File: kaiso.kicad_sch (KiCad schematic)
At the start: 404 parts, among them J1 Conn_01x04, J2 Conn_01x05, J3 Conn_01x02, J4 Conn_01x02, SW0_18 Mechanical_Switch, SW0_19 Mechanical_Switch, SW0_20 Mechanical_Switch, SW0_21 Mechanical_Switch, SW0_22 Mechanical_Switch, SW0_23 Mechanical_Switch, SW0_24 Mechanical_Switch, SW0_25 Mechanical_Switch, SW0_26 Mechanical_Switch, SW0_27 Mechanical_Switch, SW0_28 Mechanical_Switch, SW0_29 Mechanical_Switch, SW0_30 Mechanical_Switch, SW0_31 Mechanical_Switch, SW0_32 Mechanical_Switch, SW0_33 Mechanical_Switch, SW0_34 Mechanical_Switch, SW0_35 Mechanical_Switch, SW1_14 Mechanical_Switch, SW1_18 Mechanical_Switch, SW1_19 Mechanical_Switch, SW1_20 Mechanical_Switch, SW1_21 Mechanical_Switch, SW1_22 Mechanical_Switch, SW1_23 Mechanical_Switch, SW1_24 Mechanical_Switch, SW1_25 Mechanical_Switch, SW1_26 Mechanical_Switch, SW1_27 Mechanical_Switch, SW1_28 Mechanical_Switch, SW1_29 Mechanical_Switch, SW1_30 Mechanical_Switch, SW1_31 Mechanical_Switch, SW1_32 Mechanical_Switch, SW1_33 Mechanical_Switch, SW2_14 Mechanical_Switch, SW2_18 Mechanical_Switch, SW2_19 Mechanical_Switch, SW2_20 Mechanical_Switch, SW2_21 Mechanical_Switch, SW2_22 Mechanical_Switch, SW2_23 Mechanical_Switch, SW2_24 Mechanical_Switch, SW2_25 Mechanical_Switch, SW2_26 Mechanical_Switch, SW2_27 Mechanical_Switch, SW2_28 Mechanical_Switch, SW2_29 Mechanical_Switch, SW2_30 Mechanical_Switch, SW2_31 Mechanical_Switch, SW2_32 Mechanical_Switch, SW2_33 Mechanical_Switch, SW3_13 Mechanical_Switch, SW3_14 Mechanical_Switch, SW3_18 Mechanical_Switch, SW3_19 Mechanical_Switch, SW3_20 Mechanical_Switch, SW3_21 Mechanical_Switch, SW3_22 Mechanical_Switch, SW3_23 Mechanical_Switch, SW3_24 Mechanical_Switch, SW3_25 Mechanical_Switch, SW3_26 Mechanical_Switch, SW3_27 Mechanical_Switch, SW3_28 Mechanical_Switch, SW3_29 Mechanical_Switch, SW3_30 Mechanical_Switch, SW3_31 Mechanical_Switch, SW4_11 Mechanical_Switch, SW4_14 Mechanical_Switch, SW4_18 Mechanical_Switch, SW4_19 Mechanical_Switch, SW4_20 Mechanical_Switch, SW4_21 Mechanical_Switch, SW4_22 Mechanical_Switch, SW4_23 Mechanical_Switch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

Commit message: Finished the schematic REV 1
Still need to update the switch schematic symbol and double check the boot and reset pins
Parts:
- removed J2: Conn_01x05, symbol Connector_Generic:Conn_01x05
- added C10, C11: 1uF, symbol Device:C
- added C12, C13: 10pF, symbol Device:C
- added C9: 10nF, symbol Device:C
- added D1: RED, symbol Device:LED
- added FB1: 120R, symbol Device:FerriteBead
- added J2: Conn_01x04_Pin, symbol Connector:Conn_01x04_Pin
- added R3: 1.5k, symbol Device:R_US
- added Y1: 16MHz, symbol Device:Crystal_GND24
- J1: value Conn_01x04 -> JST_SH_Conn_01x04; footprint Connector_Molex:Molex_Pico-EZmate_78171-0004_1x04-1MP_P1.20mm_Vertical -> Connector_JST:JST_SH_BM04B-SRSS-TB_1x04-1MP_P1.00mm_Vertical
- LED1: value SK6812MINI-E -> Esc
- LED10: value SK6812MINI-E -> F9
- LED100: value SK6812MINI-E -> Fn
- LED101, LED91: value SK6812MINI-E -> Ctrl
- LED103: value SK6812MINI-E -> Left
- LED104: value SK6812MINI-E -> Down
- LED106: value SK6812MINI-E -> Right
- LED107, LED29: value SK6812MINI-E -> 0
- LED108: value SK6812MINI-E -> .
- LED11: value SK6812MINI-E -> F10
- LED12: value SK6812MINI-E -> F11
- LED13: value SK6812MINI-E -> F12
- LED14: value SK6812MINI-E -> Home/End
- LED15: value SK6812MINI-E -> Del/Ins
- LED16: value SK6812MINI-E -> PgUp/PgDn
- LED17, LED83: value SK6812MINI-E -> /
- LED18: value SK6812MINI-E -> *
- LED19: value SK6812MINI-E -> `
- LED2: value SK6812MINI-E -> F1
- LED20, LED88: value SK6812MINI-E -> 1
- LED21, LED89: value SK6812MINI-E -> 2
- LED22, LED90: value SK6812MINI-E -> 3
- LED23, LED70: value SK6812MINI-E -> 4
- LED24, LED71: value SK6812MINI-E -> 5
- LED25, LED72: value SK6812MINI-E -> 6
- LED26, LED52: value SK6812MINI-E -> 7
- LED27, LED53: value SK6812MINI-E -> 8
- LED28, LED54: value SK6812MINI-E -> 9
- LED3: value SK6812MINI-E -> F2
- LED30, LED36: value SK6812MINI-E -> -
- LED31: value SK6812MINI-E -> =
- LED32: value SK6812MINI-E -> Backspace
- LED34: value SK6812MINI-E -> Num Lk
- LED35: value SK6812MINI-E -> +
- LED37: value SK6812MINI-E -> Tab
- LED38: value SK6812MINI-E -> q
- LED39: value SK6812MINI-E -> w
- LED4: value SK6812MINI-E -> F3
- LED40: value SK6812MINI-E -> e
- LED41: value SK6812MINI-E -> r
- LED42: value SK6812MINI-E -> t
- LED43: value SK6812MINI-E -> y
- LED44: value SK6812MINI-E -> u
- LED45: value SK6812MINI-E -> i
- LED46: value SK6812MINI-E -> o
- LED47: value SK6812MINI-E -> P
- LED48: value SK6812MINI-E -> [
- LED49: value SK6812MINI-E -> ]
- LED5: value SK6812MINI-E -> F4
- LED50: value SK6812MINI-E -> Enter
- LED55: value SK6812MINI-E -> Caps Lock
- LED56: value SK6812MINI-E -> a
- LED57: value SK6812MINI-E -> s
- LED58: value SK6812MINI-E -> d
- LED59: value SK6812MINI-E -> f
- LED6: value SK6812MINI-E -> F5
- LED60: value SK6812MINI-E -> g
- LED61: value SK6812MINI-E -> h
- LED62: value SK6812MINI-E -> j
- LED63: value SK6812MINI-E -> k
- LED64: value SK6812MINI-E -> L
- LED65: value SK6812MINI-E -> ;
- LED66: value SK6812MINI-E -> '
- LED67: value SK6812MINI-E -> \
- LED7: value SK6812MINI-E -> F6
- LED73, LED85: value SK6812MINI-E -> Shift
- LED74: value SK6812MINI-E -> z
- LED75: value SK6812MINI-E -> x
- LED76: value SK6812MINI-E -> c
- LED77: value SK6812MINI-E -> v
- LED78: value SK6812MINI-E -> b
- LED79: value SK6812MINI-E -> n
- LED8: value SK6812MINI-E -> F7
- LED80: value SK6812MINI-E -> m
- LED81: value SK6812MINI-E -> <
- LED82: value SK6812MINI-E -> >
- LED86: value SK6812MINI-E -> Up
- LED9: value SK6812MINI-E -> F8
- LED92: value SK6812MINI-E -> Super
- LED93, LED99: value SK6812MINI-E -> Alt
- LED96: value SK6812MINI-E -> Space
- SW0_18: Keycode ESC -> KC
- SW5_23: Keycode . Prt Sc -> KC
- SW5_4: Keycode Win -> KC
- SW5_6: Keycode Alt -> KC
- U1: value STM32F103C8Tx -> STM32F103C8T6
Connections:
- net INTB is gone; now on net COL6: U1.25 (PB12)
- net SCL is gone; now on net COL4: U1.21 (PB10)
- net SDA is gone; now on net COL5: U1.22 (PB11)
- net SDB is gone; now on net COL7: U1.26 (PB13)
- net +3.3V: now also C11.1, D1.2 (A), FB1.2, J2.1 (Pin_1); no longer U1.9 (VDDA)
- net COL0: no longer SW0_18.1
- net COL1: no longer SW5_4.1
- net COL10: now also U1.10 (PA0); no longer U1.14 (PA4)
- net COL11: now also U1.11 (PA1); no longer U1.15 (PA5)
- net COL12: now also U1.12 (PA2); no longer U1.16 (PA6)
- net COL13: now also U1.13 (PA3); no longer U1.17 (PA7)
- net COL14: now also U1.14 (PA4); no longer U1.29 (PA8)
- net COL15: now also U1.15 (PA5); no longer U1.30 (PA9)
- net COL16: now also U1.16 (PA6); no longer U1.31 (PA10)
- net COL17: now also U1.17 (PA7); no longer SW0_35.1, U1.38 (PA15)
- net COL4: no longer U1.27 (PB14)
- net COL5: no longer U1.28 (PB15)
- net COL6: no longer U1.10 (PA0)
- net COL7: no longer U1.11 (PA1)
- net COL8: now also U1.27 (PB14); no longer U1.12 (PA2)
- net COL9: now also U1.28 (PB15); no longer U1.13 (PA3)
- net GND: now also C10.2, C11.2, C12.2, C13.2, C9.2, J2.4 (Pin_4), R3.2, Y1.2, Y1.4
- net RGB: now also U1.30 (PA9)
- net SWCLK: now also J2.3 (Pin_3)
- net SWDIO: now also J2.2 (Pin_2)
- net HSE_IN: now reaches U1.5 (PD0)
- net HSE_IN: now also C12.1, Y1.1
- net HSE_OUT: now reaches U1.6 (PD1)
- net HSE_OUT: now also C13.1, Y1.3
- net at D90.2 (A): no longer SW5_4.2
- net at D24.2 (A): no longer SW0_18.2
- net D+ renamed USB_D+
- net D- renamed USB_D-
- new net: D1.1 (K), R3.1
- new net +3.3VA: C10.1, C9.1, FB1.1, U1.9 (VDDA)
- no-connect marks 0 -> 7
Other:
- removed sheet LED_Matrix
- note added: "CL=2*(CL0-Cs)=2*(10-5)pF=10pF"
- note added: "Crystal Oscillator"
- note added: "Decoupling Capacitor for VA"
- note removed: "Switch Matrix"
- title: KiKeeb -> Kaiso92
- moved on the sheet: C1, C100, C101, C103, C104, C105, C106, C107, C108, C111, C114, C115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

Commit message: updated the switch matrix symbols and fixed some violations.
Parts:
- removed D109, D110, D111, D112, D113, D114, D115, D116, D117, D118, D119, D120, D121, D122, D123, D124, D125, D126, D127, D128, D129, D130, D131, D132, D133, D134, D135, D136, D137, D138, D139, D140, D141, D142, D143, D144, D145, D146, D147, D148, D149, D150, D151, D152, D153, D154, D155, D156, D157, D158, D159, D160, D161, D162, D163, D164, D165, D166, D167, D168, D169, D170, D171, D172, D173, D174, D175, D176, D177, D178, D179, D180, D181, D182, D183, D184, D185, D186, D187, D188, D189, D190, D191, D192: 1N4148W, Diode_SMD:D_SOD-123, symbol Diode:1N4148W
- removed SW0_19, SW0_20, SW0_21, SW0_22, SW0_23, SW0_24, SW0_25, SW0_26, SW0_27, SW0_28, SW0_29, SW0_30, SW0_31, SW0_32, SW0_33, SW0_34, SW0_35, SW1_14, SW1_18, SW1_19, SW1_20, SW1_21, SW1_22, SW1_23, SW1_24, SW1_25, SW1_26, SW1_27, SW1_28, SW1_29, SW1_30, SW1_31, SW1_32, SW1_33, SW2_18, SW2_19, SW2_20, SW2_21, SW2_22, SW2_23, SW2_24, SW2_25, SW2_26, SW2_27, SW2_28, SW2_29, SW2_30, SW2_31, SW2_32, SW2_33, SW3_14, SW3_18, SW3_19, SW3_20, SW3_21, SW3_22, SW3_23, SW3_24, SW3_25, SW3_26, SW3_27, SW3_28, SW3_29, SW3_30, SW3_31, SW4_14, SW4_18, SW4_19, SW4_20, SW4_21, SW4_22, SW4_23, SW4_24, SW4_25, SW4_26, SW4_28, SW4_29, SW4_30, SW4_31, SW5_14, SW5_18, SW5_19, SW5_20, SW5_21, SW5_22, SW5_23, SW5_7: Mechanical_Switch, PCM_marbastlib-mx:SW_MX_1u, symbol acheron_Symbols:Mechanical_Switch
- removed SW2_14: Mechanical_Switch, PCM_marbastlib-mx:SW_MX_1.5u, symbol acheron_Symbols:Mechanical_Switch
- removed SW3_13, SW4_27: Mechanical_Switch, PCM_marbastlib-mx:SW_MX_1.75u, symbol acheron_Symbols:Mechanical_Switch
- removed SW5_3, SW5_4, SW5_6: Mechanical_Switch, PCM_marbastlib-mx:SW_MX_1.25u, symbol acheron_Symbols:Mechanical_Switch
- added D10, D11, D12, D13, D14, D15, D16, D17, D18, D19, D20, D21, D22, D23, D24, D25, D26, D27, D28, D29, D3, D31, D32, D33, D34, D35, D36, D37, D38, D39, D4, D40, D41, D43, D44, D45, D46, D47, D49, D5, D50, D51, D52, D53, D54, D55, D56, D57, D58, D59, D6, D60, D61, D62, D63, D64, D65, D66, D67, D68, D69, D7, D70, D73, D74, D75, D76, D77, D78, D79, D8, D80, D81, D83, D84, D85, D9, D91, D92, D93, D94, D95, D96, D97: 1N4148W, Diode_SMD:D_SOD-123, symbol Diode:1N4148W
- added SW0_1, SW0_10, SW0_11, SW0_12, SW0_13, SW0_14, SW0_15, SW0_16, SW0_17, SW0_2, SW0_3, SW0_4, SW0_5, SW0_6, SW0_7, SW0_8, SW0_9, SW1_0, SW1_1, SW1_10, SW1_11, SW1_12, SW1_13, SW1_15, SW1_16, SW1_17, SW1_2, SW1_3, SW1_4, SW1_5, SW1_6, SW1_7, SW1_8, SW1_9, SW2_1, SW2_10, SW2_11, SW2_12, SW2_13, SW2_15, SW2_16, SW2_17, SW2_2, SW2_3, SW2_4, SW2_5, SW2_6, SW2_7, SW2_8, SW2_9, SW3_1, SW3_10, SW3_11, SW3_12, SW3_15, SW3_16, SW3_17, SW3_2, SW3_3, SW3_4, SW3_5, SW3_6, SW3_7, SW3_8, SW3_9, SW4_0, SW4_1, SW4_10, SW4_12, SW4_15, SW4_16, SW4_17, SW4_2, SW4_3, SW4_4, SW4_5, SW4_6, SW4_7, SW4_8, SW4_9, SW5_10, SW5_12, SW5_15, SW5_16, SW5_17, SW5_5, SW5_8, SW5_9: Mechanical_Switch, PCM_marbastlib-mx:SW_MX_1u, symbol acheron_Symbols:Mechanical_Switch
- added SW2_0: Mechanical_Switch, PCM_marbastlib-mx:SW_MX_1.5u, symbol acheron_Symbols:Mechanical_Switch
- added SW3_0: Mechanical_Switch, PCM_marbastlib-mx:SW_MX_1.75u, symbol acheron_Symbols:Mechanical_Switch
- added SW5_0, SW5_1, SW5_2: Mechanical_Switch, PCM_marbastlib-mx:SW_MX_1.25u, symbol acheron_Symbols:Mechanical_Switch
- SW0_0: renamed from SW0_18; Keycode KC -> ESC
- SW4_11: footprint PCM_marbastlib-mx:SW_MX_1u -> PCM_marbastlib-mx:SW_MX_1.75u
- SW5_11: Keycode Alt -> Left
- renumbered D24 to D2
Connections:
- net COL0: now also SW0_0.1, SW1_0.1, SW2_0.1, SW3_0.1, SW4_0.1, SW5_0.1; no longer SW4_11.1
- net COL1: now also SW0_1.1, SW1_1.1, SW2_1.1, SW3_1.1, SW4_1.1, SW5_1.1
- net COL10: now also SW0_10.1, SW1_10.1, SW2_10.1, SW3_10.1, SW4_10.1, SW5_10.1
- net COL11: now also SW4_11.1, SW5_11.1, SW0_11.1, SW1_11.1, SW2_11.1, SW3_11.1
- net COL12: now also SW0_12.1, SW1_12.1, SW2_12.1, SW3_12.1, SW4_12.1, SW5_12.1
- net COL13: now also SW0_13.1, SW1_13.1, SW2_13.1
- net COL14: now also SW0_14.1
- net COL15: now also SW0_15.1, SW1_15.1, SW2_15.1, SW3_15.1, SW4_15.1, SW5_15.1
- net COL16: now also SW0_16.1, SW1_16.1, SW2_16.1, SW3_16.1, SW4_16.1, SW5_16.1
- net COL17: now also SW0_17.1, SW1_17.1, SW2_17.1, SW3_17.1, SW4_17.1, SW5_17.1
- net COL2: now also SW0_2.1, SW1_2.1, SW2_2.1, SW3_2.1, SW4_2.1, SW5_2.1
- net COL3: now also SW0_3.1, SW1_3.1, SW2_3.1, SW3_3.1, SW4_3.1
- net COL4: now also SW0_4.1, SW1_4.1, SW2_4.1, SW3_4.1, SW4_4.1
- net COL5: now also SW0_5.1, SW1_5.1, SW2_5.1, SW3_5.1, SW4_5.1, SW5_5.1
- net COL6: now also SW0_6.1, SW1_6.1, SW2_6.1, SW3_6.1, SW4_6.1
- net COL7: now also SW0_7.1, SW1_7.1, SW2_7.1, SW3_7.1, SW4_7.1
- net COL8: now also SW0_8.1, SW1_8.1, SW2_8.1, SW3_8.1, SW4_8.1, SW5_8.1; no longer SW5_11.1
- net COL9: now also SW0_9.1, SW1_9.1, SW2_9.1, SW3_9.1, SW4_9.1, SW5_9.1
- net ROW0: now also D10.1 (K), D11.1 (K), D12.1 (K), D13.1 (K), D14.1 (K), D15.1 (K), D16.1 (K), D17.1 (K), D18.1 (K), D19.1 (K), D3.1 (K), D4.1 (K), D5.1 (K), D6.1 (K), D7.1 (K), D8.1 (K), D9.1 (K); no longer D82.1 (K)
- net ROW1: now also D20.1 (K), D21.1 (K), D22.1 (K), D23.1 (K), D24.1 (K), D25.1 (K), D26.1 (K), D27.1 (K), D28.1 (K), D29.1 (K), D31.1 (K), D32.1 (K), D33.1 (K), D34.1 (K), D35.1 (K), D36.1 (K); no longer D86.1 (K)
- net ROW2: now also D48.1 (K), D37.1 (K), D38.1 (K), D39.1 (K), D40.1 (K), D41.1 (K), D43.1 (K), D44.1 (K), D45.1 (K), D46.1 (K), D47.1 (K), D49.1 (K), D50.1 (K), D51.1 (K), D52.1 (K), D53.1 (K); no longer D87.1 (K)
- net ROW3: now also D54.1 (K), D55.1 (K), D56.1 (K), D57.1 (K), D58.1 (K), D59.1 (K), D60.1 (K), D61.1 (K), D62.1 (K), D63.1 (K), D64.1 (K), D65.1 (K), D66.1 (K), D67.1 (K), D68.1 (K), D69.1 (K); no longer D48.1 (K), D88.1 (K)
- net ROW4: now also D72.1 (K), D82.1 (K), D70.1 (K), D73.1 (K), D74.1 (K), D75.1 (K), D76.1 (K), D77.1 (K), D78.1 (K), D79.1 (K), D80.1 (K), D81.1 (K), D83.1 (K), D84.1 (K), D85.1 (K); no longer D89.1 (K)
- net ROW5: now also D86.1 (K), D87.1 (K), D88.1 (K), D89.1 (K), D91.1 (K), D92.1 (K), D93.1 (K), D94.1 (K), D95.1 (K), D96.1 (K), D97.1 (K); no longer D72.1 (K)
- net at D87.2 (A): now also SW5_1.2
- net at D48.2 (A): now also SW2_11.2
- net at D82.2 (A): now also SW4_12.2
- net at D88.2 (A): now also SW5_2.2
- net at D42.2 (A): now also SW2_5.2
- net at D71.2 (A): now also SW4_1.2; no longer SW4_11.2
- net at D86.2 (A): now also SW5_0.2
- net at SW5_11.2: now also D93.2 (A)
- net at D89.2 (A): now also SW5_5.2
- net at D90.2 (A): now also SW5_8.2
- net at D2.2 (A): now also SW0_0.2
- net at D30.2 (A): now also SW1_10.2
- net at D72.2 (A): now also SW4_2.2
- new net: D38.2 (A), SW2_1.2
- new net: D36.2 (A), SW1_17.2
- new net: D76.2 (A), SW4_6.2
- new net: D43.2 (A), SW2_6.2
- new net: D27.2 (A), SW1_7.2
- new net: D75.2 (A), SW4_5.2
- new net: D17.2 (A), SW0_15.2
- new net: D78.2 (A), SW4_8.2
- new net: D51.2 (A), SW2_15.2
- new net: D74.2 (A), SW4_4.2
- new net: D10.2 (A), SW0_8.2
- new net: D60.2 (A), SW3_6.2
- new net: D85.2 (A), SW4_17.2
- new net: D35.2 (A), SW1_16.2
- new net: D97.2 (A), SW5_17.2
- new net: D8.2 (A), SW0_6.2
- new net: D32.2 (A), SW1_12.2
- new net: D21.2 (A), SW1_1.2
- new net: D39.2 (A), SW2_2.2
- new net: D24.2 (A), SW1_4.2
- new net: D70.2 (A), SW4_0.2
- new net: D47.2 (A), SW2_10.2
- new net: D50.2 (A), SW2_13.2
- new net: D96.2 (A), SW5_16.2
- new net: D81.2 (A), SW4_11.2
- new net: D34.2 (A), SW1_15.2
- new net: D80.2 (A), SW4_10.2
- new net: D4.2 (A), SW0_2.2
- new net: D49.2 (A), SW2_12.2
- new net: D46.2 (A), SW2_9.2
- new net: D22.2 (A), SW1_2.2
- new net: D91.2 (A), SW5_9.2
- new net: D77.2 (A), SW4_7.2
- new net: D25.2 (A), SW1_5.2
- new net: D59.2 (A), SW3_5.2
- new net: D41.2 (A), SW2_4.2
- new net: D53.2 (A), SW2_17.2
- new net: D45.2 (A), SW2_8.2
- new net: D92.2 (A), SW5_10.2
- new net: D6.2 (A), SW0_4.2
- new net: D95.2 (A), SW5_15.2
- new net: D64.2 (A), SW3_10.2
- new net: D20.2 (A), SW1_0.2
- new net: D83.2 (A), SW4_15.2
- new net: D37.2 (A), SW2_0.2
- new net: D40.2 (A), SW2_3.2
- new net: D54.2 (A), SW3_0.2
- new net: D28.2 (A), SW1_8.2
- new net: D11.2 (A), SW0_9.2
- new net: D73.2 (A), SW4_3.2
- new net: D13.2 (A), SW0_11.2
- new net: D5.2 (A), SW0_3.2
- new net: D12.2 (A), SW0_10.2
- new net: D44.2 (A), SW2_7.2
- new net: D7.2 (A), SW0_5.2
- new net: D18.2 (A), SW0_16.2
- new net: D33.2 (A), SW1_13.2
- new net: D3.2 (A), SW0_1.2
- new net: D19.2 (A), SW0_17.2
- new net: D69.2 (A), SW3_17.2
- new net: D94.2 (A), SW5_12.2
- new net: D29.2 (A), SW1_9.2
- new net: D66.2 (A), SW3_12.2
- new net: D15.2 (A), SW0_13.2
- new net: D56.2 (A), SW3_2.2
- new net: D23.2 (A), SW1_3.2
- new net: D61.2 (A), SW3_7.2
- new net: D14.2 (A), SW0_12.2
- new net: D31.2 (A), SW1_11.2
- new net: D62.2 (A), SW3_8.2
- new net: D79.2 (A), SW4_9.2
- new net: D57.2 (A), SW3_3.2
- new net: D52.2 (A), SW2_16.2
- new net: D58.2 (A), SW3_4.2
- new net: D67.2 (A), SW3_15.2
- new net: D84.2 (A), SW4_16.2
- new net: D63.2 (A), SW3_9.2
- new net: D55.2 (A), SW3_1.2
- new net: D65.2 (A), SW3_11.2
- new net: D26.2 (A), SW1_6.2
- new net: D68.2 (A), SW3_16.2
- new net: D16.2 (A), SW0_14.2
- new net: D9.2 (A), SW0_7.2
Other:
- note added: "SK6812mini-e LED Chain"
- note added: "Switch Matrix"
- moved on the sheet: C1, C10, C100, C101, C103, C104, C105, C106, C107, C108, C11, C111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

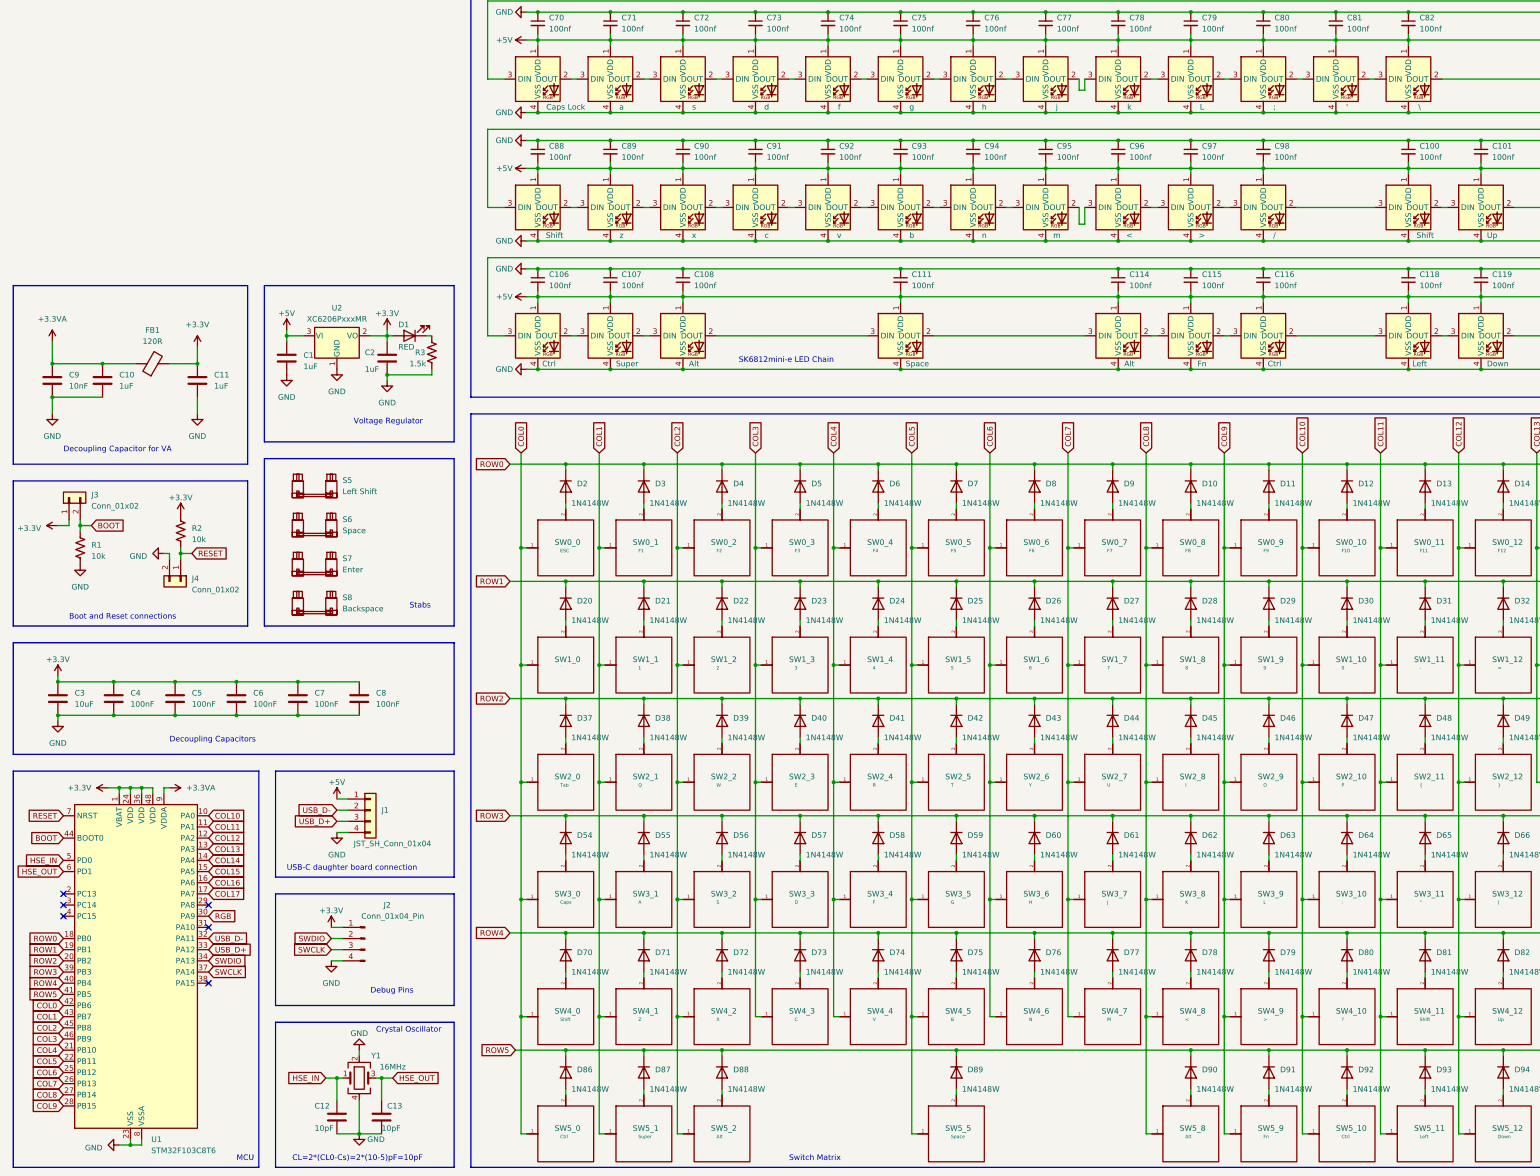
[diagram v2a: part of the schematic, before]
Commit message: updated footprints
Updated SPDT sch and finished adding all the footprints to all the sch symbols. Everything's good to move to the PCB editor.
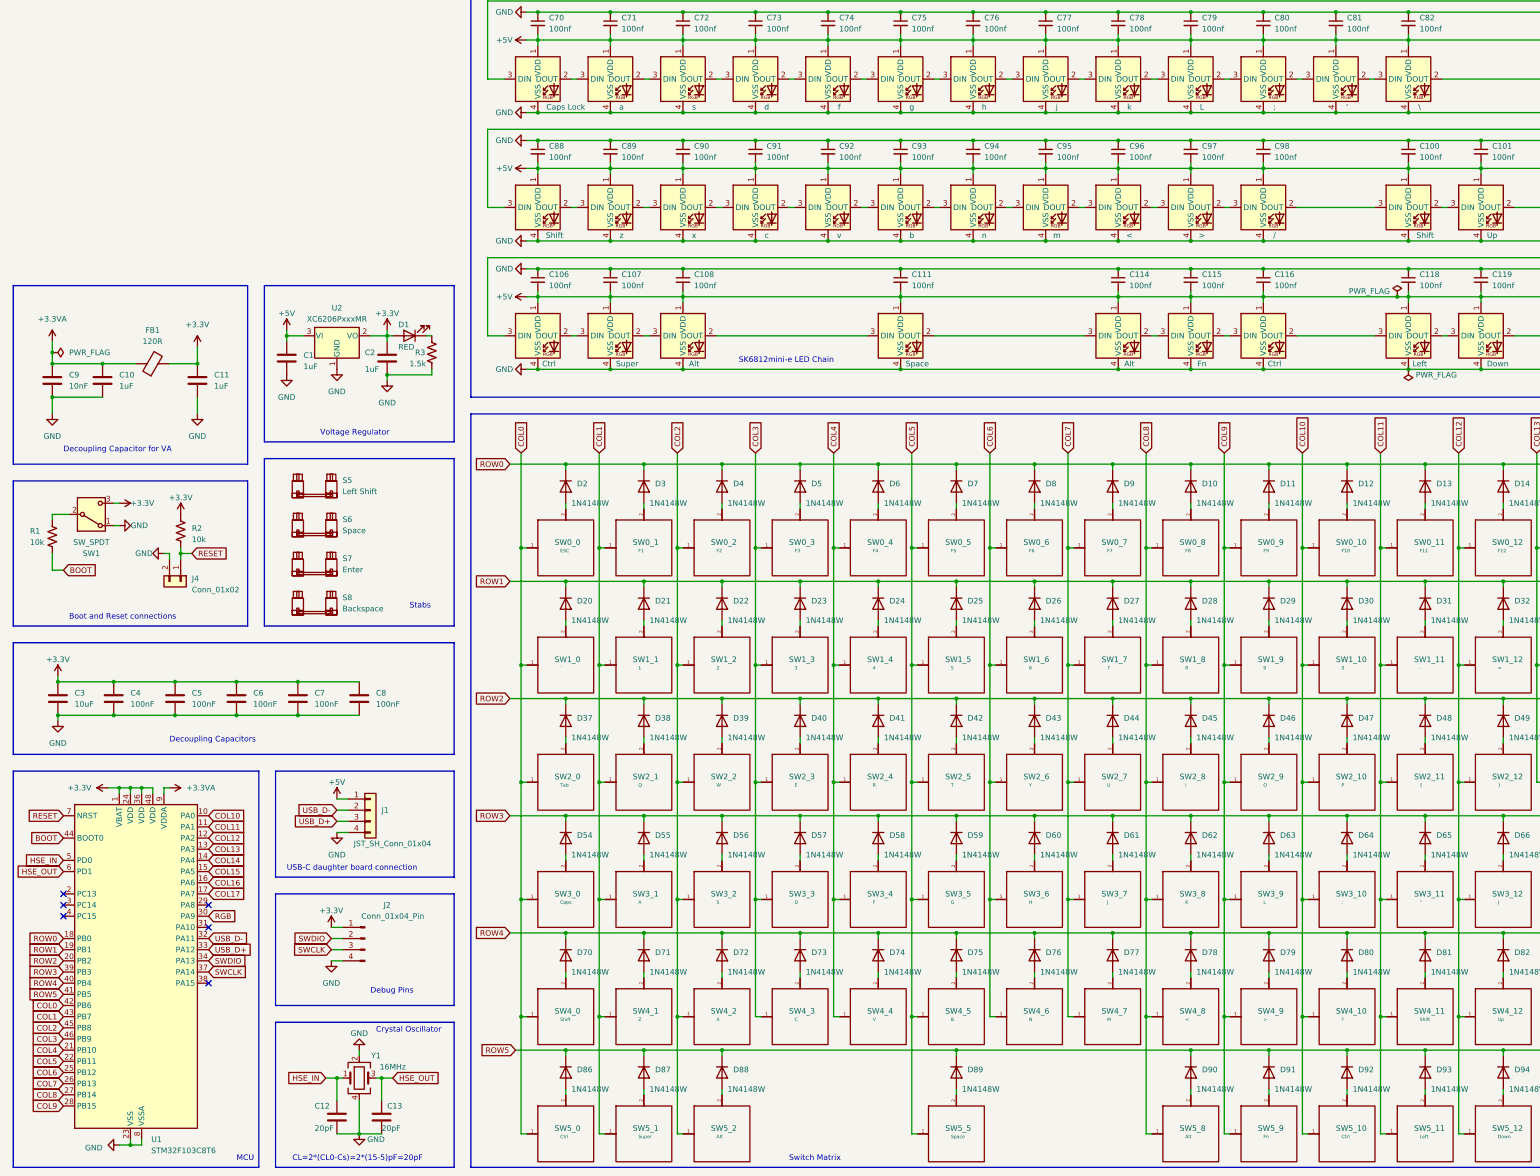
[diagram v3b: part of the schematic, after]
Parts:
- removed J3: Conn_01x02, symbol Connector_Generic:Conn_01x02
- added SW1: SW_SPDT, SW:SW-TH_SK12D07VG3, symbol Switch:SW_SPDT
- C1, C10, C100, C101, C103, C104, C105, C106, C107, C108, C11, C111, C114, C115, C116, C118, C119, C121, C122, C123, C16, C17, C18, C19, C2, C20, C21, C22, C23, C24, C25, C26, C27, C28, C29, C30, C31, C32, C33, C34, C35, C36, C37, C38, C39, C4, C40, C41, C42, C43, C44, C45, C46, C47, C49, C5, C50, C51, C52, C53, C54, C55, C56, C57, C58, C59, C6, C60, C61, C62, C63, C64, C65, C67, C68, C69, C7, C70, C71, C72, C73, C74, C75, C76, C77, C78, C79, C8, C80, C81, C82, C85, C86, C87, C88, C89, C90, C91, C92, C93, C94, C95, C96, C97, C98: footprint (none) -> Capacitor_SMD:C_0402_1005Metric
- C12, C13: value 10pF -> 20pF; footprint (none) -> Capacitor_SMD:C_0201_0603Metric
- C3, C9: footprint (none) -> Capacitor_SMD:C_0603_1608Metric
- D1: footprint (none) -> LED_SMD:LED_0603_1608Metric
- FB1: footprint (none) -> Inductor_SMD:L_0603_1608Metric
- J2: footprint (none) -> Connector_PinHeader_2.54mm:PinHeader_1x04_P2.54mm_Vertical
- J4: footprint (none) -> Connector_PinHeader_2.54mm:PinHeader_1x02_P2.54mm_Vertical
- R1, R2, R3: footprint (none) -> Resistor_SMD:R_0402_1005Metric
- Y1: footprint (none) -> Crystal:Resonator_SMD_Murata_CSTxExxV-3Pin_3.0x1.1mm
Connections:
- net +3.3V: now also SW1.3 (C)
- net BOOT: now also R1.2; no longer R1.1
- net GND: now also SW1.1 (A); no longer R1.2
- new net: R1.1, SW1.2 (B)
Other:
- note added: "CL=2*(CL0-Cs)=2*(15-5)pF=20pF"
- note removed: "CL=2*(CL0-Cs)=2*(10-5)pF=10pF"
- moved on the sheet: R1
